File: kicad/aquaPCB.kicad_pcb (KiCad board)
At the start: 2 copper layers, 100 x 100 mm, 188 parts, among them J1 12V IN, J19 1-wire DS1820, J2 Raspberry Pi, J22 I2C 1, J23 I2C 2, J24 Display, J26 ADC #1 in 2, J27 ADC #1 in 3, J28 DC ports, J29 LED ports, J30 PCA9685 #1 ch 0, J31 Float 1, J32 Float 2, J33 Power bar 1, J34 Power bar 2, J35 Sensors, J36 I2C 5V, J37 ADC #1 in 0, J38 ADC #1 in 1, J4 PWM 0, J5 GPIO 12, J6 GPIO 13, J7 PWM 1, J8 GPIO 16, J9 GPIO 26, Q1 AOD4184A, Q10 AOD4185, Q11 AO3400A, Q2 AOD4184A, Q3 AOD4184A, Q4 AOD4184A, Q5 AOD4184A, Q6 AOD4184A, U1 TPS54360B, U10 PCA9685PW, U11 PCA9306D, U2 AMS1117-3.3, U3 74HCT244D, U5 ADS1115IDGSR, U7 PCA9685PW, U8 74HCT244D, U9 74HCT244D

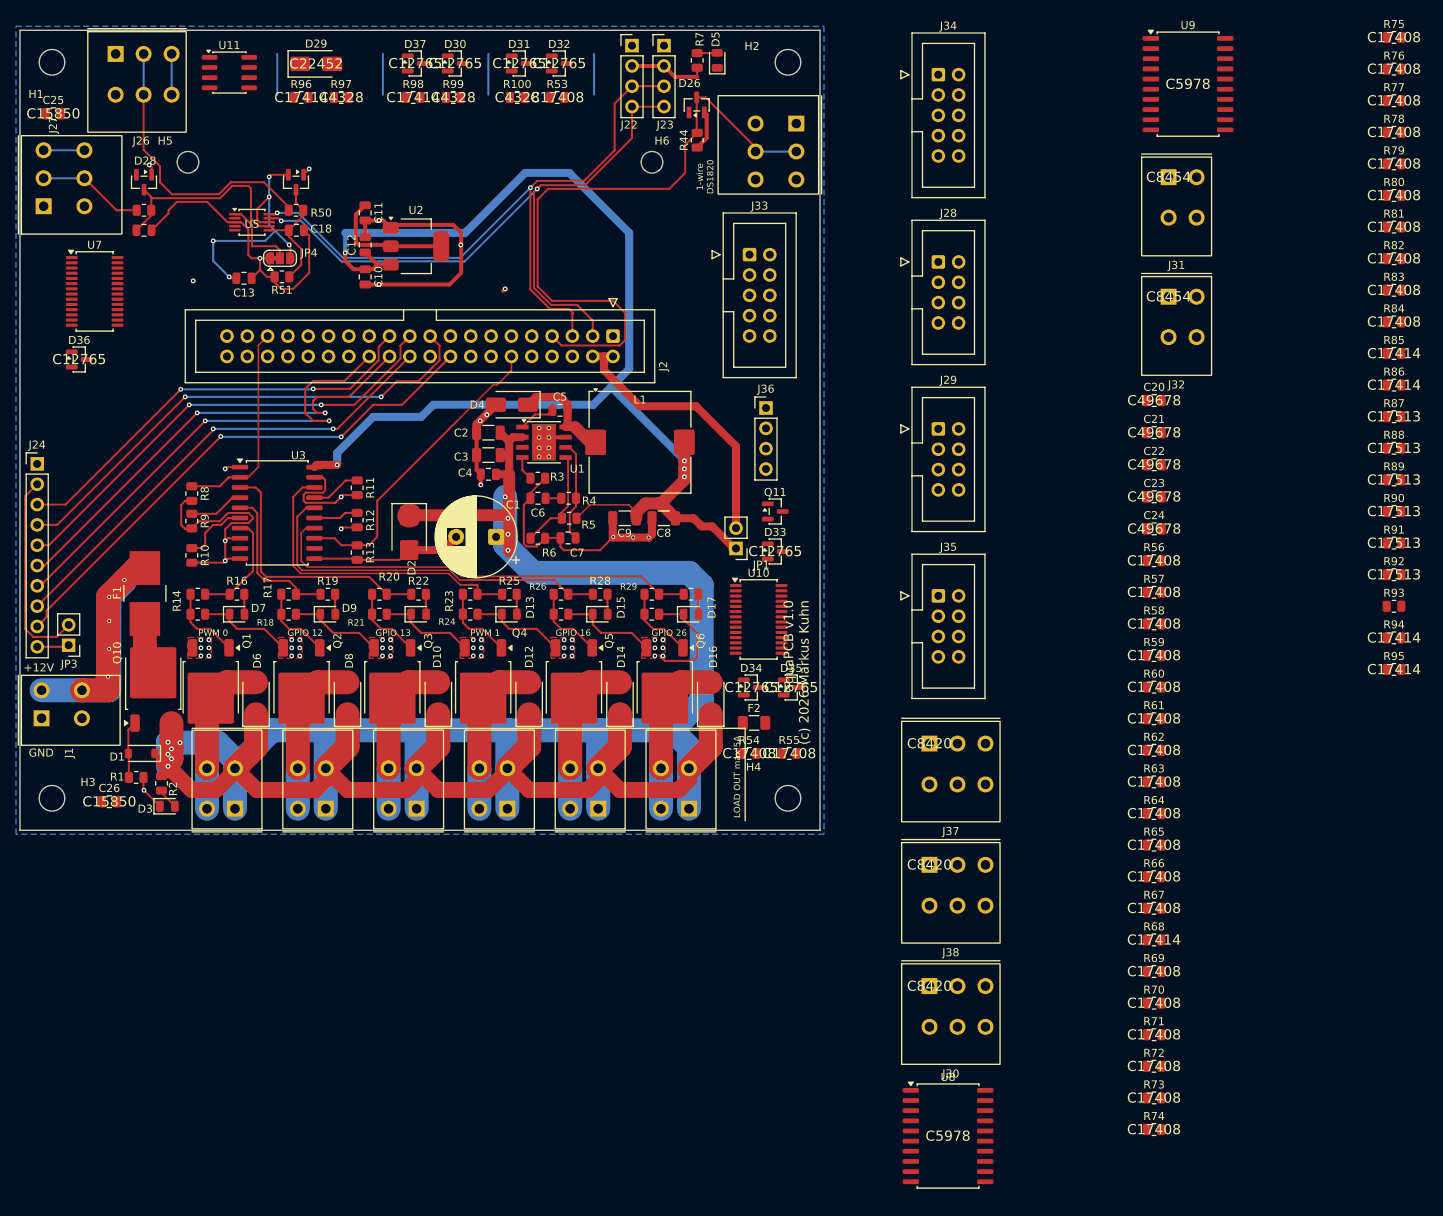
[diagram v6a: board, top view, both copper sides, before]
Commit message: kicad: v2 space measures - feeder on power bar header, resistor arrays, 0603, TSSOP buffers
Feeder port dropped: power bar header pin 10 = +3V3_EXT (own AMS1117), any PCA #2 channel as signal; 30 series resistors as 8x 4x0603 arrays; new passives 0603; new 74HCT244 in TSSOP-20; flat parts may use the Pi zone, connectors anywhere else. ERC 0, DRC copper 0, parity 0.

Co-Authored-By: Claude Opus 5.5 <noreply@anthropic.com>
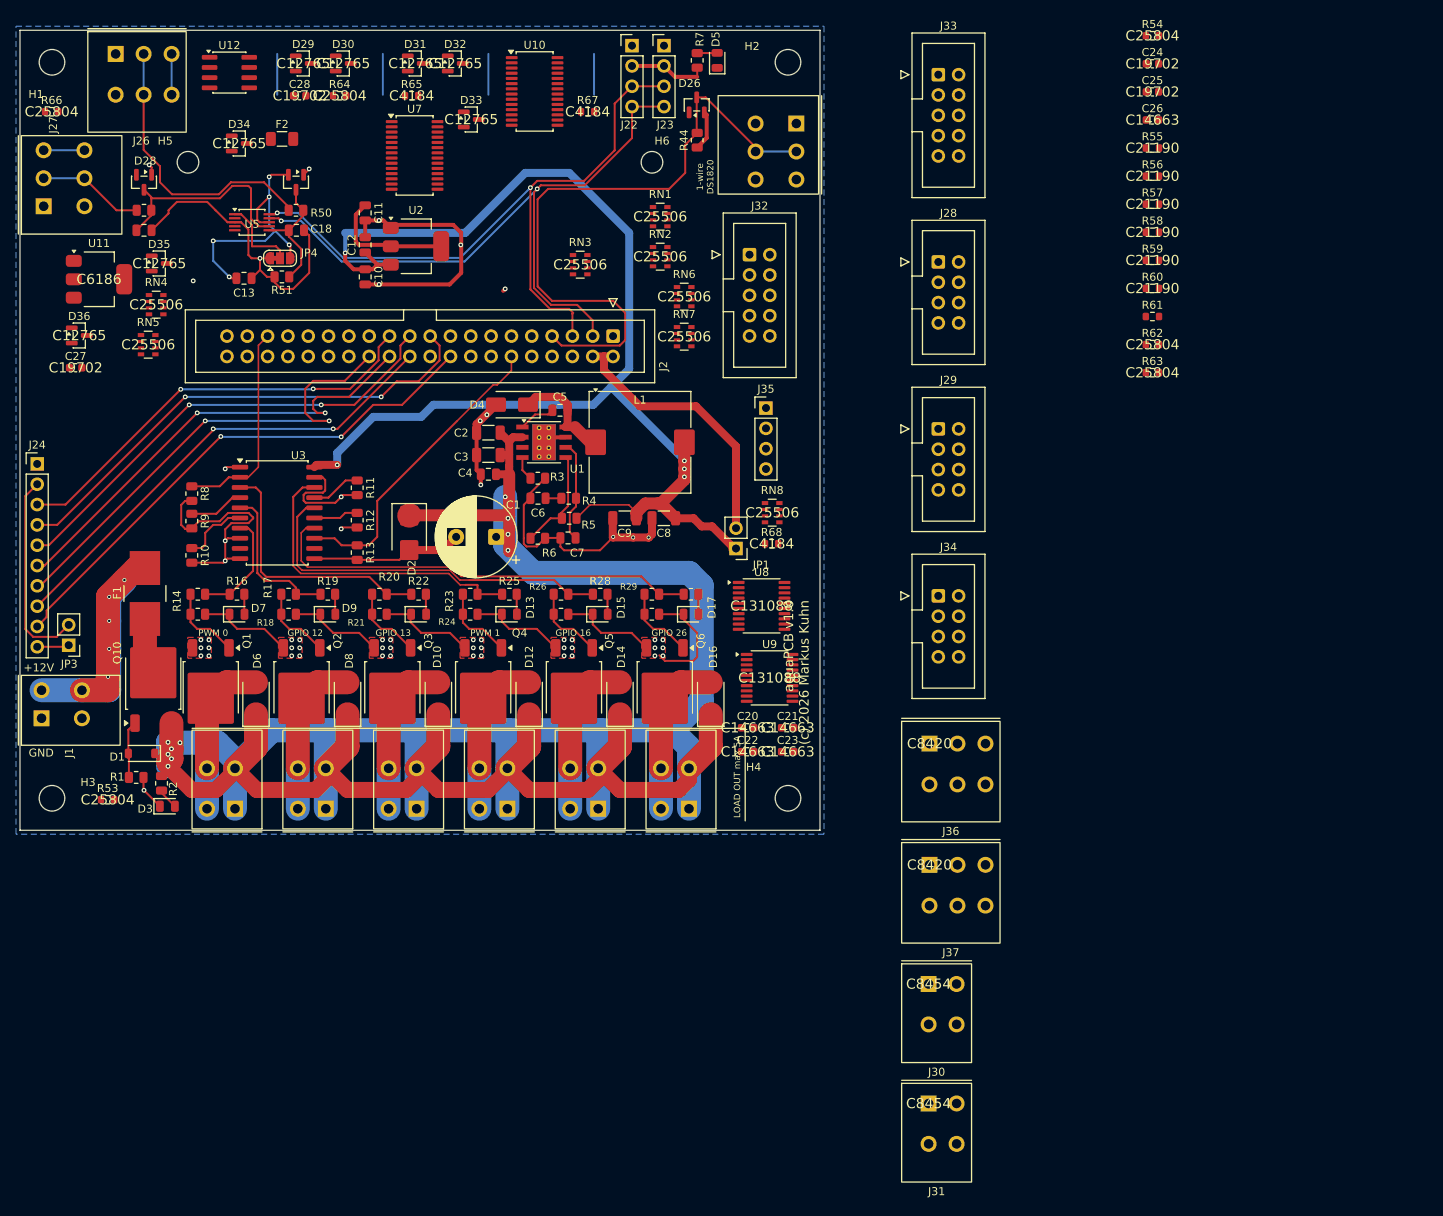
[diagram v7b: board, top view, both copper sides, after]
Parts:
- removed D37: BAT54S, Package_TO_SOT_SMD:SOT-23
- removed J38: ADC #1 in 1, aquaPCB:TerminalBlock_Kangnex_WJ250B-3.5-03P_P3.50mm_Staggered
- removed Q11: AO3400A, Package_TO_SOT_SMD:SOT-23
- removed R100, R97, R99: 20k, Resistor_SMD:R_0805_2012Metric
- removed R69, R70, R71, R72, R73, R74, R75, R76, R77, R78, R79, R80, R81, R82, R83, R84: 100, Resistor_SMD:R_0805_2012Metric
- removed R85, R86, R94, R95, R96, R98: 10k, Resistor_SMD:R_0805_2012Metric
- removed R87, R88, R89, R90, R91, R92: 1k, Resistor_SMD:R_0805_2012Metric
- removed R93: 200k, Resistor_SMD:R_0805_2012Metric
- added C27: 10u, Capacitor_SMD:C_0603_1608Metric, F.Cu at (85.8, 77.9)
- added C28: 10u, Capacitor_SMD:C_0603_1608Metric, F.Cu at (113.8, 43.9)
- added RN1: 4x100, Resistor_SMD:R_Array_Convex_4x0603, F.Cu at (158.9, 59.0)
- added RN2: 4x100, Resistor_SMD:R_Array_Convex_4x0603, F.Cu at (158.9, 64.0)
- added RN3: 4x100, Resistor_SMD:R_Array_Convex_4x0603, F.Cu at (148.9, 65.0)
- added RN4: 4x100, Resistor_SMD:R_Array_Convex_4x0603, F.Cu at (95.9, 70.0)
- added RN5: 4x100, Resistor_SMD:R_Array_Convex_4x0603, F.Cu at (94.9, 75.0)
- added RN6: 4x100, Resistor_SMD:R_Array_Convex_4x0603, F.Cu at (161.9, 69.0)
- added RN7: 4x100, Resistor_SMD:R_Array_Convex_4x0603, F.Cu at (161.9, 74.0)
- added RN8: 4x100, Resistor_SMD:R_Array_Convex_4x0603, F.Cu at (172.9, 96.0)
- added U12: PCA9306D, Package_SO:SOIC-8_3.9x4.9mm_P1.27mm, F.Cu at (105.0, 41.0)
- C20, C21, C22, C23, C25: footprint Capacitor_SMD:C_0805_2012Metric -> Capacitor_SMD:C_0603_1608Metric
- C24: value 100n -> 10u; footprint Capacitor_SMD:C_0805_2012Metric -> Capacitor_SMD:C_0603_1608Metric
- C26: value 10u -> 100n; footprint Capacitor_SMD:C_0805_2012Metric -> Capacitor_SMD:C_0603_1608Metric
- D29: value SS54 -> BAT54S; footprint Diode_SMD:D_SMA -> Package_TO_SOT_SMD:SOT-23
- J30: value PCA9685 #1 ch 0 -> Float 1; footprint aquaPCB:TerminalBlock_Kangnex_WJ250B-3.5-03P_P3.50mm_Staggered -> aquaPCB:TerminalBlock_Kangnex_WJ250B-3.5-02P_P3.50mm_Staggered
- J31: value Float 1 -> Float 2
- J32: value Float 2 -> Power bar 1; footprint aquaPCB:TerminalBlock_Kangnex_WJ250B-3.5-02P_P3.50mm_Staggered -> Connector_IDC:IDC-Header_2x05_P2.54mm_Vertical
- J33: value Power bar 1 -> Power bar 2
- J34: value Power bar 2 -> Sensors; footprint Connector_IDC:IDC-Header_2x05_P2.54mm_Vertical -> Connector_IDC:IDC-Header_2x04_P2.54mm_Vertical
- J35: value Sensors -> I2C 5V; footprint Connector_IDC:IDC-Header_2x04_P2.54mm_Vertical -> Connector_PinHeader_2.54mm:PinHeader_1x04_P2.54mm_Vertical
- J36: value I2C 5V -> ADC #1 in 0; footprint Connector_PinHeader_2.54mm:PinHeader_1x04_P2.54mm_Vertical -> aquaPCB:TerminalBlock_Kangnex_WJ250B-3.5-03P_P3.50mm_Staggered
- J37: value ADC #1 in 0 -> ADC #1 in 1
- R53, R54, R62, R63, R64, R66: value 100 -> 10k; footprint Resistor_SMD:R_0805_2012Metric -> Resistor_SMD:R_0603_1608Metric
- R55, R56, R57, R58, R59, R60: value 100 -> 1k; footprint Resistor_SMD:R_0805_2012Metric -> Resistor_SMD:R_0603_1608Metric
- R61: value 100 -> 200k; footprint Resistor_SMD:R_0805_2012Metric -> Resistor_SMD:R_0603_1608Metric
- R65, R67: value 100 -> 20k; footprint Resistor_SMD:R_0805_2012Metric -> Resistor_SMD:R_0603_1608Metric
- R68: value 10k -> 20k; footprint Resistor_SMD:R_0805_2012Metric -> Resistor_SMD:R_0603_1608Metric
- U11: value PCA9306D -> AMS1117-3.3; footprint Package_SO:SOIC-8_3.9x4.9mm_P1.27mm -> Package_TO_SOT_SMD:SOT-223-3_TabPin2
- U8, U9: value 74HCT244D -> 74HCT244PW; footprint Package_SO:SOIC-20W_7.5x12.8mm_P1.27mm -> Package_SO:TSSOP-20_4.4x6.5mm_P0.65mm
- moved R66 167.7 mm to (82.8, 45.9)
- moved C26 155.8 mm to (220.4, 46.9)
- moved C25 137.4 mm to (220.4, 43.4)
- moved R64 135.7 mm to (118.8, 43.9)
- moved R65 131.9 mm to (127.8, 43.9)
- moved R67 122.2 mm to (149.8, 45.9)
- moved J31 119.6 mm to (192.4, 169.8)
- moved R53 104.2 mm to (89.8, 131.9)
- moved R54 102.9 mm to (220.4, 36.4)
- moved D35 95.1 mm to (96.3, 64.8)
- moved F2 93.9 mm to (111.6, 49.3)
- moved D34 93.4 mm to (106.3, 49.8)
- moved U9 90.8 mm to (172.6, 116.6)
- moved R55 88.3 mm to (220.4, 50.4)
- moved U10 71.7 mm to (143.2, 43.3)
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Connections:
- C24 pad 1: /Sensor inputs, +5V_EXT, 5 V I2C/I2C5_REF -> +5V_EXT
- C25 pad 1: /ADS1115 ADC and analog sockets/AIN0 -> +3V3_EXT
- C26 pad 1: /ADS1115 ADC and analog sockets/AIN1 -> /Sensor inputs, +5V_EXT, 5 V I2C/I2C5_REF
- D29 pad 1: +3V3 -> GND
- D29 pad 2: /PWM outputs: PCA9685 #1, DC + LED ports, feeder/FEED_SW -> +3V3
- D30 pad 3: GPIO5_SENS1 -> GPIO6_SENS2
- D31 pad 3: GPIO6_SENS2 -> GPIO20_SENS3
- D32 pad 3: GPIO20_SENS3 -> GPIO21_SENS4
- D33 pad 3: GPIO21_SENS4 -> GPIO22_SENS5
- D34 pad 3: GPIO22_SENS5 -> GPIO23_SENS6
- D35 pad 3: GPIO23_SENS6 -> /ADS1115 ADC and analog sockets/AIN0
- D36 pad 3: /ADS1115 ADC and analog sockets/AIN0 -> /ADS1115 ADC and analog sockets/AIN1
- J30 pad 1: +3V3 -> /Power bars: PCA9685 #2, float backups/FLOAT1_IN
- J30 pad 2: /PWM outputs: PCA9685 #1, DC + LED ports, feeder/FEED_SW -> /Power bars: PCA9685 #2, float backups/BAR1_CH1
- J31 pad 1: /Power bars: PCA9685 #2, float backups/FLOAT1_IN -> /Power bars: PCA9685 #2, float backups/FLOAT2_IN
- J31 pad 2: /Power bars: PCA9685 #2, float backups/BAR1_CH1 -> /Power bars: PCA9685 #2, float backups/BAR1_CH2
- J32 pad 1: /Power bars: PCA9685 #2, float backups/FLOAT2_IN -> /Power bars: PCA9685 #2, float backups/BAR1_CH1
- J32 pad 2: /Power bars: PCA9685 #2, float backups/BAR1_CH2 -> /Power bars: PCA9685 #2, float backups/BAR1_CH8
- J33 pad 1: /Power bars: PCA9685 #2, float backups/BAR1_CH1 -> /Power bars: PCA9685 #2, float backups/BAR2_CH1
- J33 pad 10: unconnected-(J33-Pin_10-Pad10) -> +3V3_EXT
- J33 pad 2: /Power bars: PCA9685 #2, float backups/BAR1_CH8 -> /Power bars: PCA9685 #2, float backups/BAR2_CH8
- J33 pad 3: /Power bars: PCA9685 #2, float backups/BAR1_CH2 -> /Power bars: PCA9685 #2, float backups/BAR2_CH2
- J33 pad 4: /Power bars: PCA9685 #2, float backups/BAR1_CH7 -> /Power bars: PCA9685 #2, float backups/BAR2_CH7
- J33 pad 5: /Power bars: PCA9685 #2, float backups/BAR1_CH3 -> /Power bars: PCA9685 #2, float backups/BAR2_CH3
- J33 pad 6: /Power bars: PCA9685 #2, float backups/BAR1_CH6 -> /Power bars: PCA9685 #2, float backups/BAR2_CH6
- J33 pad 7: /Power bars: PCA9685 #2, float backups/BAR1_CH4 -> /Power bars: PCA9685 #2, float backups/BAR2_CH4
- J33 pad 8: /Power bars: PCA9685 #2, float backups/BAR1_CH5 -> /Power bars: PCA9685 #2, float backups/BAR2_CH5
- J34 pad 1: /Power bars: PCA9685 #2, float backups/BAR2_CH1 -> GND
- J34 pad 2: /Power bars: PCA9685 #2, float backups/BAR2_CH8 -> /Sensor inputs, +5V_EXT, 5 V I2C/S6_IN
- J34 pad 3: /Power bars: PCA9685 #2, float backups/BAR2_CH2 -> /Sensor inputs, +5V_EXT, 5 V I2C/S5_IN
- J34 pad 4: /Power bars: PCA9685 #2, float backups/BAR2_CH7 -> /Sensor inputs, +5V_EXT, 5 V I2C/S4_IN
- J34 pad 5: /Power bars: PCA9685 #2, float backups/BAR2_CH3 -> /Sensor inputs, +5V_EXT, 5 V I2C/S3_IN
- J34 pad 6: /Power bars: PCA9685 #2, float backups/BAR2_CH6 -> /Sensor inputs, +5V_EXT, 5 V I2C/S2_IN
- J34 pad 7: /Power bars: PCA9685 #2, float backups/BAR2_CH4 -> /Sensor inputs, +5V_EXT, 5 V I2C/S1_IN
- J34 pad 8: /Power bars: PCA9685 #2, float backups/BAR2_CH5 -> +5V_EXT
- J35 pad 1: GND -> +5V_EXT
- J35 pad 2: /Sensor inputs, +5V_EXT, 5 V I2C/S6_IN -> /Sensor inputs, +5V_EXT, 5 V I2C/I2C5_SCL
- J35 pad 3: /Sensor inputs, +5V_EXT, 5 V I2C/S5_IN -> /Sensor inputs, +5V_EXT, 5 V I2C/I2C5_SDA
- J35 pad 4: /Sensor inputs, +5V_EXT, 5 V I2C/S4_IN -> GND
- J36 pad 2: /Sensor inputs, +5V_EXT, 5 V I2C/I2C5_SCL -> /ADS1115 ADC and analog sockets/AIN0_IN
- J36 pad 3: /Sensor inputs, +5V_EXT, 5 V I2C/I2C5_SDA -> GND
- J37 pad 2: /ADS1115 ADC and analog sockets/AIN0_IN -> /ADS1115 ADC and analog sockets/AIN1_IN
- R53 pad 1: /PWM outputs: PCA9685 #1, DC + LED ports, feeder/DC_PWM1_B -> /Power bars: PCA9685 #2, float backups/BAR1_CH1
- R53 pad 2: /PWM outputs: PCA9685 #1, DC + LED ports, feeder/DC_PWM1 -> GND
- R54 pad 1: /PWM outputs: PCA9685 #1, DC + LED ports, feeder/DC_PWM2_B -> /Power bars: PCA9685 #2, float backups/BAR1_CH2
- R54 pad 2: /PWM outputs: PCA9685 #1, DC + LED ports, feeder/DC_PWM2 -> GND
- R55 pad 1: /PWM outputs: PCA9685 #1, DC + LED ports, feeder/DC_PWM3_B -> /Sensor inputs, +5V_EXT, 5 V I2C/S1_IN
- R55 pad 2: /PWM outputs: PCA9685 #1, DC + LED ports, feeder/DC_PWM3 -> GPIO5_SENS1
- R56 pad 1: /PWM outputs: PCA9685 #1, DC + LED ports, feeder/DC_PWM4_B -> /Sensor inputs, +5V_EXT, 5 V I2C/S2_IN
- R56 pad 2: /PWM outputs: PCA9685 #1, DC + LED ports, feeder/DC_PWM4 -> GPIO6_SENS2
- R57 pad 1: /PWM outputs: PCA9685 #1, DC + LED ports, feeder/DC_PWM6_B -> /Sensor inputs, +5V_EXT, 5 V I2C/S3_IN
- R57 pad 2: /PWM outputs: PCA9685 #1, DC + LED ports, feeder/DC_PWM6 -> GPIO20_SENS3
- R58 pad 1: /PWM outputs: PCA9685 #1, DC + LED ports, feeder/DC_PWM7_B -> /Sensor inputs, +5V_EXT, 5 V I2C/S4_IN
- R58 pad 2: /PWM outputs: PCA9685 #1, DC + LED ports, feeder/DC_PWM7 -> GPIO21_SENS4
- R59 pad 1: /PWM outputs: PCA9685 #1, DC + LED ports, feeder/DC_PWM9_B -> /Sensor inputs, +5V_EXT, 5 V I2C/S5_IN
- R59 pad 2: /PWM outputs: PCA9685 #1, DC + LED ports, feeder/DC_PWM9 -> GPIO22_SENS5
- R60 pad 1: /PWM outputs: PCA9685 #1, DC + LED ports, feeder/LED_PWM8_B -> /Sensor inputs, +5V_EXT, 5 V I2C/S6_IN
- R60 pad 2: /PWM outputs: PCA9685 #1, DC + LED ports, feeder/LED_PWM8 -> GPIO23_SENS6
- R61 pad 1: /PWM outputs: PCA9685 #1, DC + LED ports, feeder/LED_PWM10_B -> +5V_EXT
- R61 pad 2: /PWM outputs: PCA9685 #1, DC + LED ports, feeder/LED_PWM10 -> /Sensor inputs, +5V_EXT, 5 V I2C/I2C5_REF
- R62 pad 1: /PWM outputs: PCA9685 #1, DC + LED ports, feeder/LED_PWM11_B -> +5V_EXT
- R62 pad 2: /PWM outputs: PCA9685 #1, DC + LED ports, feeder/LED_PWM11 -> /Sensor inputs, +5V_EXT, 5 V I2C/I2C5_SCL
- R63 pad 1: /PWM outputs: PCA9685 #1, DC + LED ports, feeder/LED_PWM12_B -> +5V_EXT
- R63 pad 2: /PWM outputs: PCA9685 #1, DC + LED ports, feeder/LED_PWM12 -> /Sensor inputs, +5V_EXT, 5 V I2C/I2C5_SDA
- R64 pad 1: /PWM outputs: PCA9685 #1, DC + LED ports, feeder/LED_PWM13_B -> /ADS1115 ADC and analog sockets/AIN0_IN
- R64 pad 2: /PWM outputs: PCA9685 #1, DC + LED ports, feeder/LED_PWM13 -> /ADS1115 ADC and analog sockets/AIN0
- R65 pad 1: /PWM outputs: PCA9685 #1, DC + LED ports, feeder/LED_PWM14_B -> /ADS1115 ADC and analog sockets/AIN0
- R65 pad 2: /PWM outputs: PCA9685 #1, DC + LED ports, feeder/LED_PWM14 -> GND
- R66 pad 1: /PWM outputs: PCA9685 #1, DC + LED ports, feeder/LED_PWM15_B -> /ADS1115 ADC and analog sockets/AIN1_IN
- R66 pad 2: /PWM outputs: PCA9685 #1, DC + LED ports, feeder/LED_PWM15 -> /ADS1115 ADC and analog sockets/AIN1
- R67 pad 1: /PWM outputs: PCA9685 #1, DC + LED ports, feeder/PCA1_CH0 -> /ADS1115 ADC and analog sockets/AIN1
- R67 pad 2: /PWM outputs: PCA9685 #1, DC + LED ports, feeder/FEED_G -> GND
- R68 pad 1: /PWM outputs: PCA9685 #1, DC + LED ports, feeder/FEED_G -> /ADS1115 ADC and analog sockets/AIN3
- U11 pad 2: +3V3 -> +3V3_EXT
- U11 pad 3: GPIO3_SCL -> +5V_EXT
- U7 pad 6: /PWM outputs: PCA9685 #1, DC + LED ports, feeder/PCA1_CH0 -> unconnected-(U7-LED0-Pad6)

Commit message: kicad: prepare v2 re-layout - keep and lock power section, remove signal routing
Power section (input protection, buck, 3V3 LDO, U3 gate driver, Q1-Q6, J4-J9, J2, holes) kept and locked: 71 footprints, 537 tracks/vias, 7 zones. Signal routing removed (241 tracks, 23 vias); 93 footprints incl. all LEDs free for re-placement. DRC copper 0, parity 0.

Co-Authored-By: Claude Opus 5.5 <noreply@anthropic.com>
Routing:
- net +3V3: track 89.7 -> 0.00 mm, vias 5 -> 0
- net GPIO3_SCL: track 86.1 -> 0.00 mm, vias 2 -> 0
- net GPIO2_SDA: track 85.4 -> 0.00 mm, vias 2 -> 0
- net GPIO4_1W: track 82.0 -> 0.00 mm
- net GPIO24_DISP_RST: track 66.2 -> 0.00 mm, vias 2 -> 0
- net GPIO10_MOSI: track 62.3 -> 0.00 mm, vias 2 -> 0
- net GPIO7_CE1: track 61.8 -> 0.00 mm, vias 2 -> 0
- net GPIO25_DISP_DC: track 59.6 -> 0.00 mm, vias 2 -> 0
- net GPIO8_CE0: track 58.5 -> 0.00 mm, vias 2 -> 0
- net GPIO9_MISO: track 58.4 -> 0.00 mm, vias 2 -> 0
- net GPIO11_SCLK: track 53.8 -> 0.00 mm, vias 2 -> 0
- net GPIO18_Q1: track 38.4 -> 0.00 mm
- net Net-(J26-Pin_2): track 35.9 -> 0.00 mm
- net GPIO19_Q4: track 26.2 -> 0.00 mm
- net /ADS1115 ADC and analog sockets/AIN3: track 25.9 -> 0.00 mm
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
